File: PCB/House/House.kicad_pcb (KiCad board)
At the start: 2 copper layers, 95 x 60.5 mm, 37 parts, among them J1 Conn_01x05, U1 HT16K33-28SOP

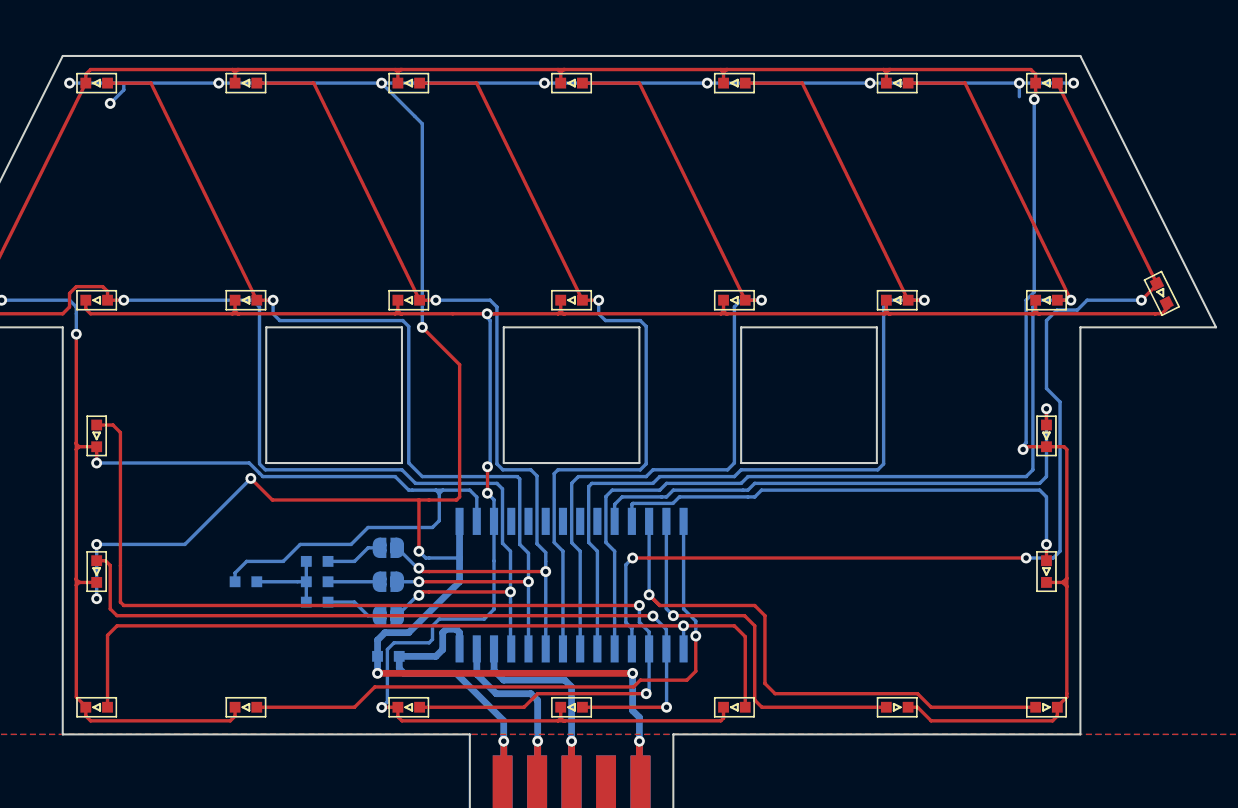
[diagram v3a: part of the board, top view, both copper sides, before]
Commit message: [update] Houseの配線改善(表面横方向配線削減)
表面横方向配線を削減した結果、
下中部に横方向の跨ぎ配線が発生。
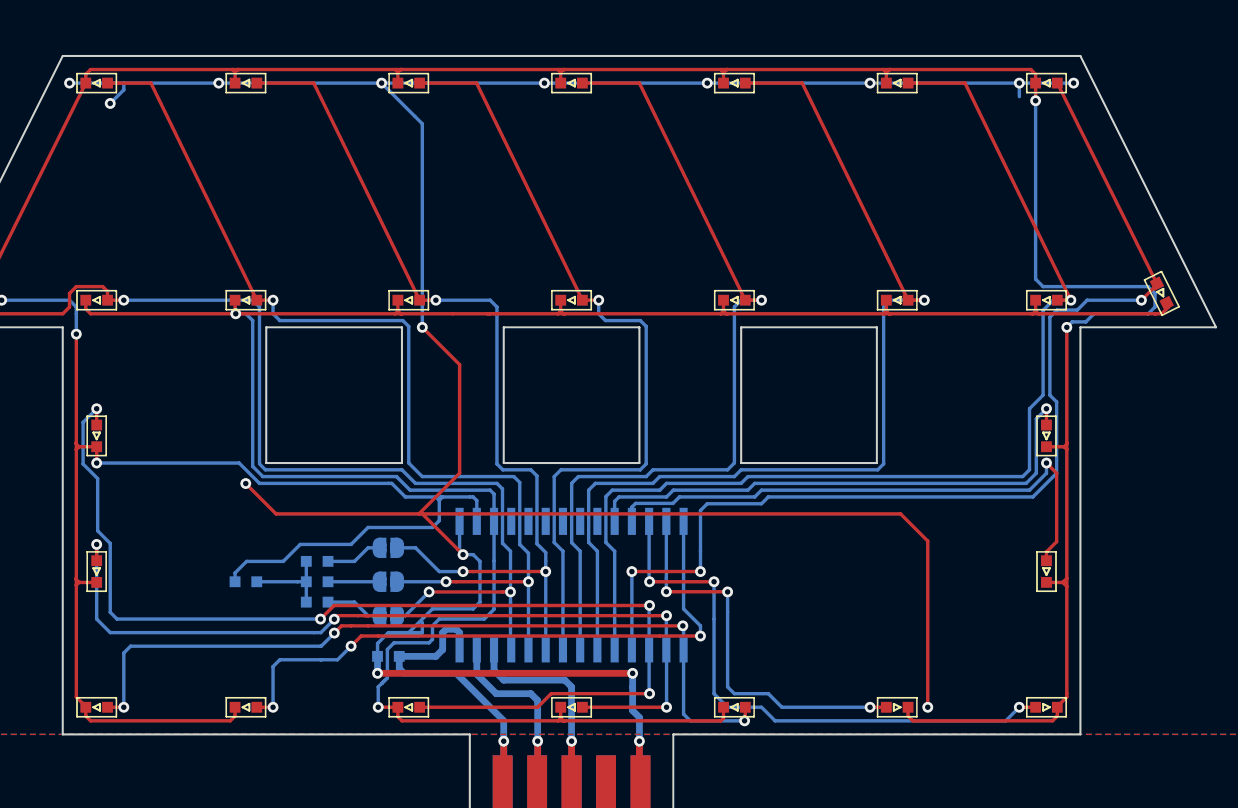
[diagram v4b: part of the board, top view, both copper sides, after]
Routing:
- net GND: track 200.1 -> 238.5 mm, vias 17 -> 16
- net Net-(D17-Pad1): track 154.9 -> 172.8 mm, vias 4 -> 2
- net Net-(D1-Pad1): track 265.5 -> 277.5 mm
- net Net-(D10-Pad2): track 57.9 -> 62.8 mm, vias 2 -> 4
- net Net-(D25-Pad2): track 76.8 -> 81.7 mm, vias 2 -> 4
- net Net-(D15-Pad2): track 37.1 -> 41.2 mm
- net Net-(D24-Pad2): track 82.0 -> 79.8 mm
- net Net-(D14-Pad2): track 41.4 -> 42.4 mm, vias 1 -> 3
- net Net-(D11-Pad2): track 59.9 -> 59.1 mm, vias 1 -> 4
- net Net-(D23-Pad2): track 81.8 -> 81.1 mm
- net Net-(D12-Pad2): track 44.9 -> 45.6 mm, vias 1 -> 3
- net Net-(D13-Pad2): track 29.1 -> 29.0 mm, vias 1 -> 3

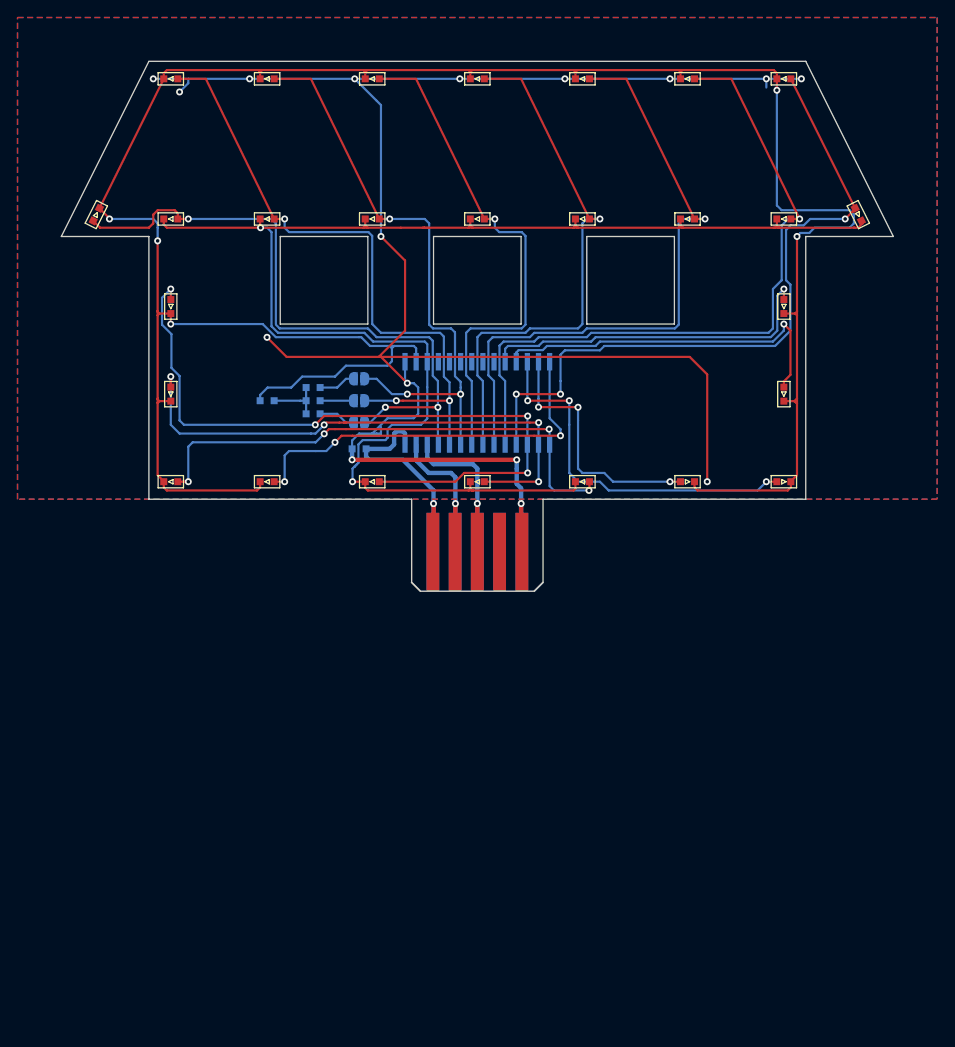
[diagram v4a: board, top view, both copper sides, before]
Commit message: [update] Houseの配線改善(表面最小化)
下中部の横方向の跨ぎ配線を極力裏面に移動。

TODO:
* I2Cアドレスパッドの表面配線を一つ横の窓に合わせる
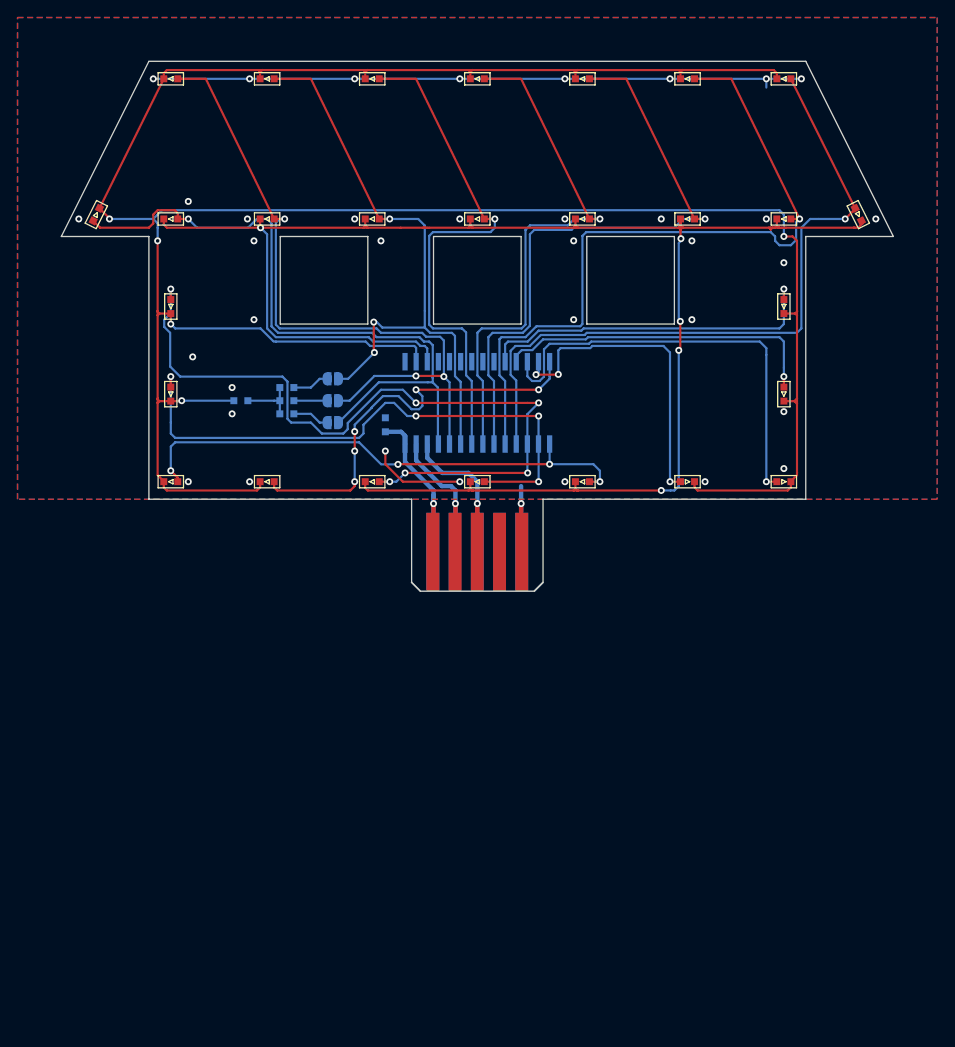
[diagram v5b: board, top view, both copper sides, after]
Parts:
- moved C1 4.07 mm to (137.0, 91.5), turned to 90 degrees
- moved D28 3.00 mm to (120.5, 88.8)
- moved JP1 3.00 mm to (131.0, 91.2)
- moved JP2 3.00 mm to (131.0, 88.8)
- moved JP3 3.00 mm to (131.0, 86.2)
- moved R1 3.00 mm to (125.8, 90.2)
- moved R2 3.00 mm to (125.8, 88.8)
- moved R3 3.00 mm to (125.8, 87.2)
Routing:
- net GND: track 238.5 -> 98.9 mm, vias 16 -> 37
- net Net-(D1-Pad1): track 277.5 -> 309.4 mm
- net Net-(D17-Pad1): track 172.8 -> 194.7 mm, vias 2 -> 5
- net Net-(D14-Pad2): track 42.4 -> 49.6 mm, vias 3 -> 1
- net Net-(D13-Pad2): track 29.0 -> 36.1 mm
- net +5V: track 30.1 -> 23.6 mm
- net Net-(D18-Pad2): track 74.4 -> 80.3 mm
- net Net-(D25-Pad2): track 81.7 -> 87.4 mm, vias 4 -> 6
- net Net-(D1-Pad2): track 74.9 -> 79.3 mm, vias 3 -> 1
- net Net-(D10-Pad2): track 62.8 -> 66.5 mm
- net Net-(D15-Pad2): track 41.2 -> 37.5 mm
- net Net-(D19-Pad2): track 67.5 -> 70.6 mm
- net Net-(D23-Pad2): track 81.1 -> 83.8 mm
- net Net-(D20-Pad2): track 58.4 -> 59.8 mm
- net Net-(D12-Pad2): track 45.6 -> 47.0 mm, vias 3 -> 5
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
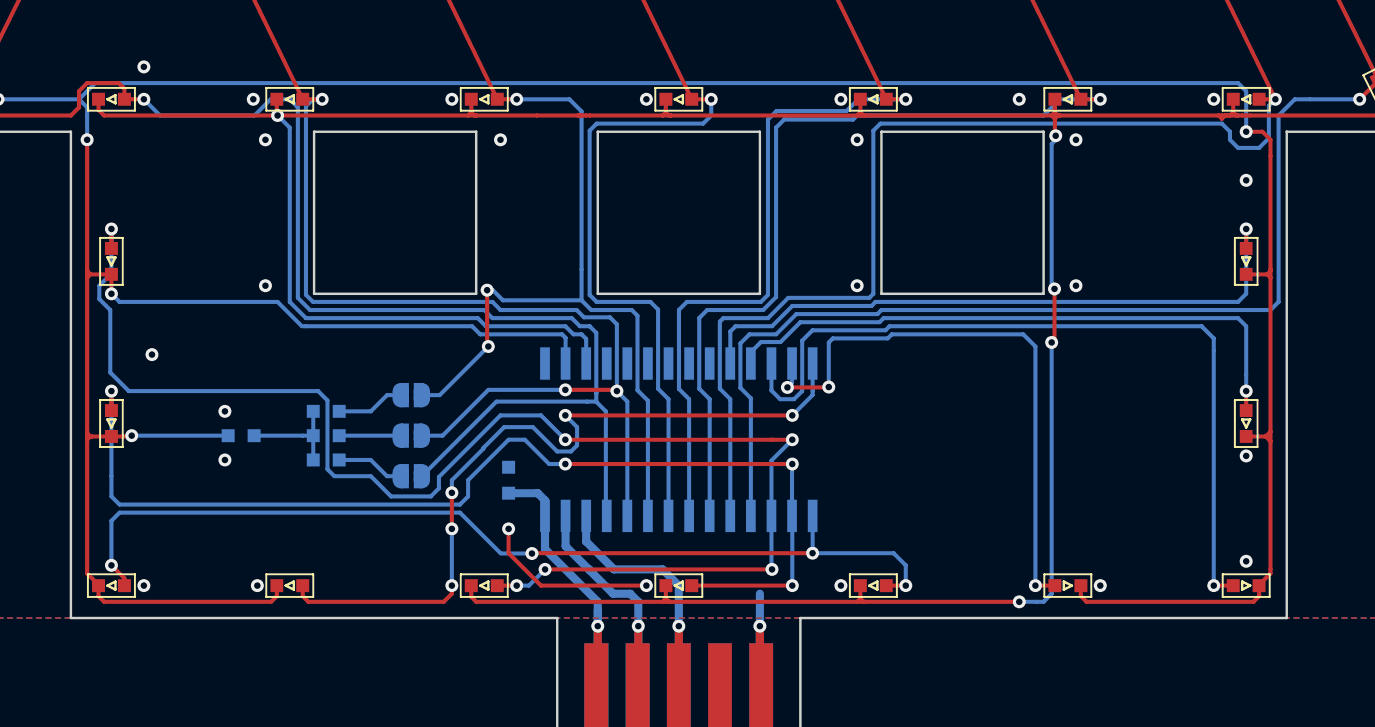
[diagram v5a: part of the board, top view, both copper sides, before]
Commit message: [update] Houseの配線改善(部品位置調整)
IC位置を窓と下部の中央に移動。
I2Cアドレスパッドとバージョンシルクも合わせて移動。
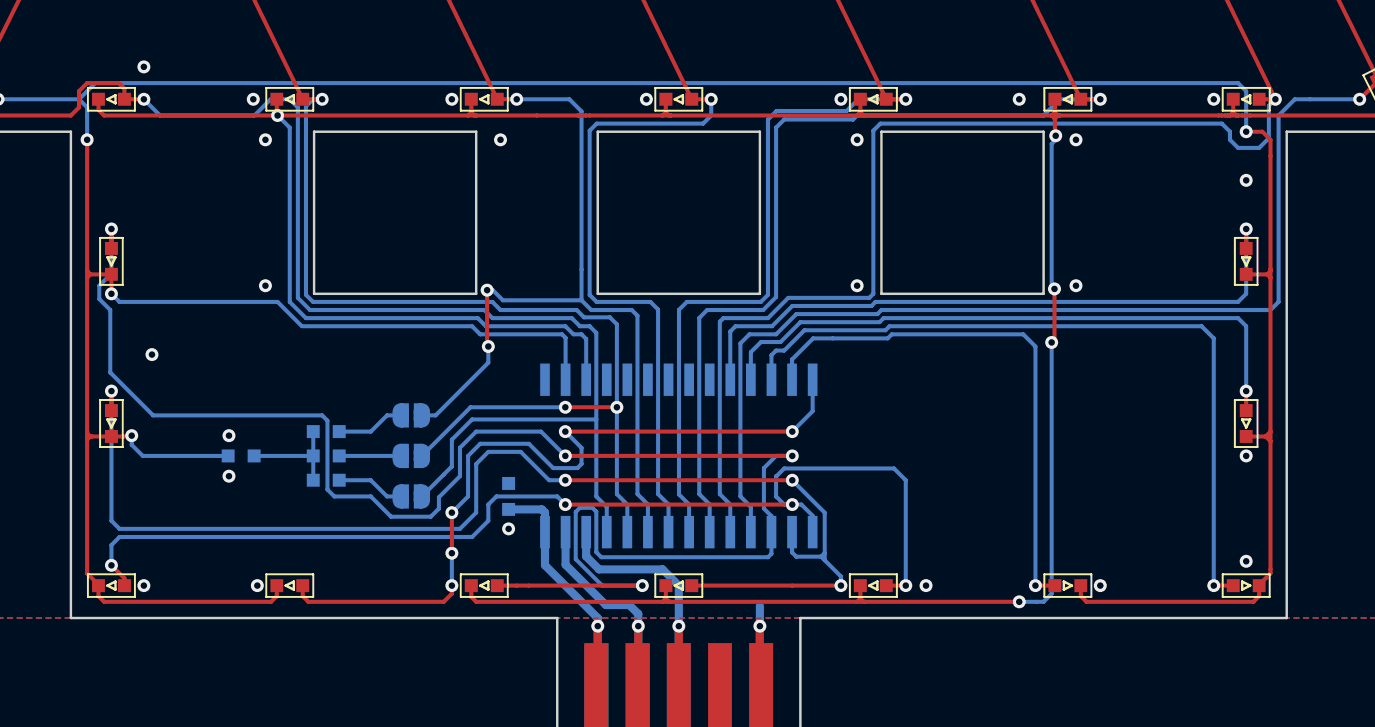
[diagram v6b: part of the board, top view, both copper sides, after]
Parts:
- moved D28 1.25 mm to (120.5, 90.0)
- moved JP1 1.25 mm to (131.0, 92.5)
- moved JP2 1.25 mm to (131.0, 90.0)
- moved JP3 1.25 mm to (131.0, 87.5)
- moved R1 1.25 mm to (125.8, 91.5)
- moved R2 1.25 mm to (125.8, 90.0)
- moved R3 1.25 mm to (125.8, 88.5)
- moved C1 1.00 mm to (137.0, 92.5)
- moved U1 1.00 mm to (147.5, 90.0)
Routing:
- net Net-(D25-Pad2): track 87.4 -> 102.3 mm, vias 6 -> 4
- net GND: track 98.9 -> 87.3 mm, vias 37 -> 36
- net Net-(D10-Pad2): track 66.5 -> 76.6 mm
- net Net-(D11-Pad2): track 59.9 -> 68.1 mm
- net Net-(D14-Pad2): track 49.6 -> 46.3 mm
- net Net-(D13-Pad2): track 36.1 -> 33.2 mm, vias 3 -> 1
- net Net-(D19-Pad2): track 70.6 -> 72.7 mm
- net Net-(D1-Pad2): track 79.3 -> 81.2 mm
- net Net-(D1-Pad1): track 309.4 -> 311.3 mm
- net Net-(D24-Pad2): track 80.3 -> 81.3 mm
- net Net-(D22-Pad2): track 72.1 -> 73.1 mm
- net Net-(D21-Pad2): track 61.9 -> 62.9 mm
- net Net-(D20-Pad2): track 59.8 -> 60.8 mm
- net Net-(D16-Pad2): track 40.0 -> 41.0 mm
- net Net-(D15-Pad2): track 37.5 -> 38.5 mm
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
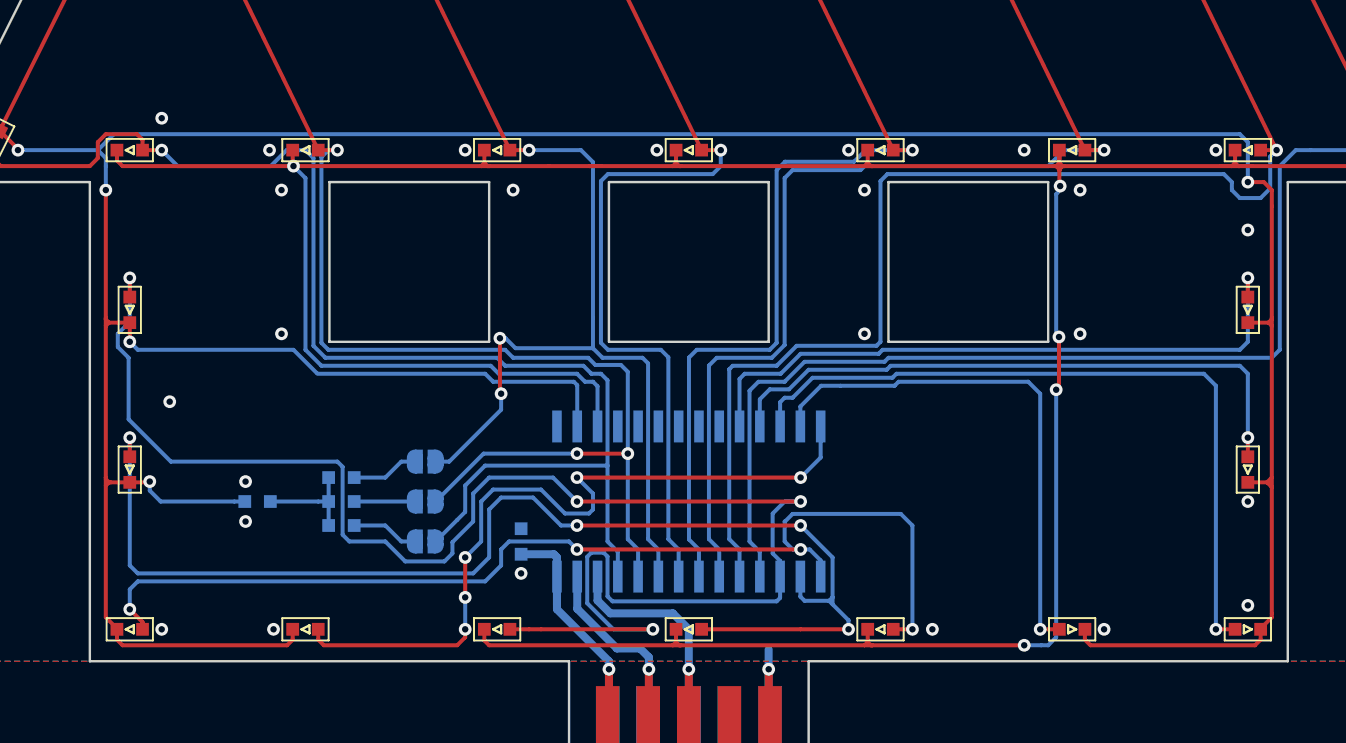
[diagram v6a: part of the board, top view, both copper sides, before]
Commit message: [update] Houseの配線改善(表面配線位置調整)
表面配線が可能な限り線対象になるように位置を調整。

TODO:
* ICの横4本配線の位置の中心化
* GNDビアの位置の調整
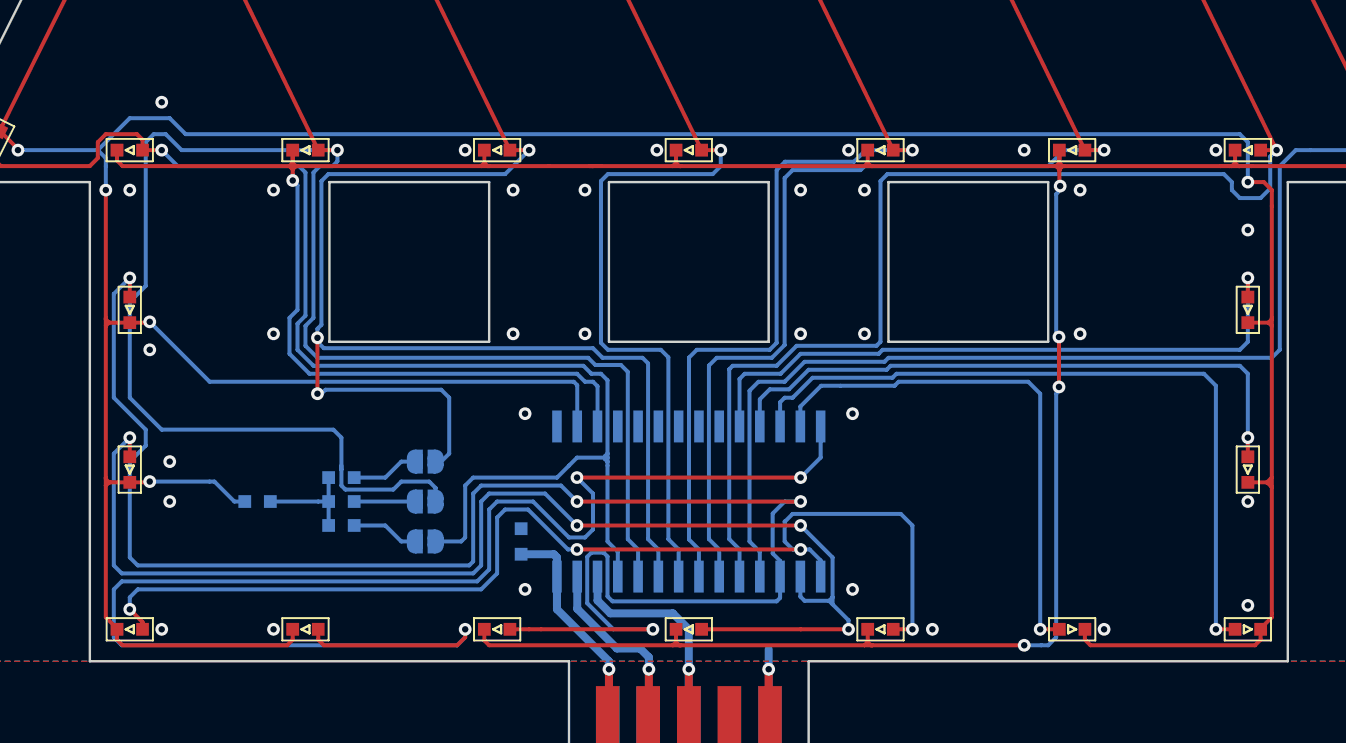
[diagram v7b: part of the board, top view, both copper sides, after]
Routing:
- net Net-(D12-Pad2): track 47.5 -> 93.9 mm, vias 5 -> 3
- net Net-(D18-Pad2): track 81.2 -> 123.5 mm, vias 3 -> 1
- net Net-(D19-Pad2): track 72.7 -> 98.7 mm
- net Net-(D25-Pad2): track 102.3 -> 106.7 mm
- net Net-(D11-Pad2): track 68.1 -> 70.9 mm
- net Net-(D17-Pad1): track 194.9 -> 197.7 mm
- net Net-(D10-Pad2): track 76.6 -> 78.8 mm
- net Net-(D1-Pad2): track 81.2 -> 82.5 mm
- net GND: vias 36 -> 44
